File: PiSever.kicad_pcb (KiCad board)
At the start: 2 copper layers, 11 parts, among them J1 USB_C_Receptacle, J2 Fan, J3 BMP, J4 RX Ant, J5 TX Ant, P1 USB_C_Plug, U1 QFM-RX1-433, U2 AK-FST

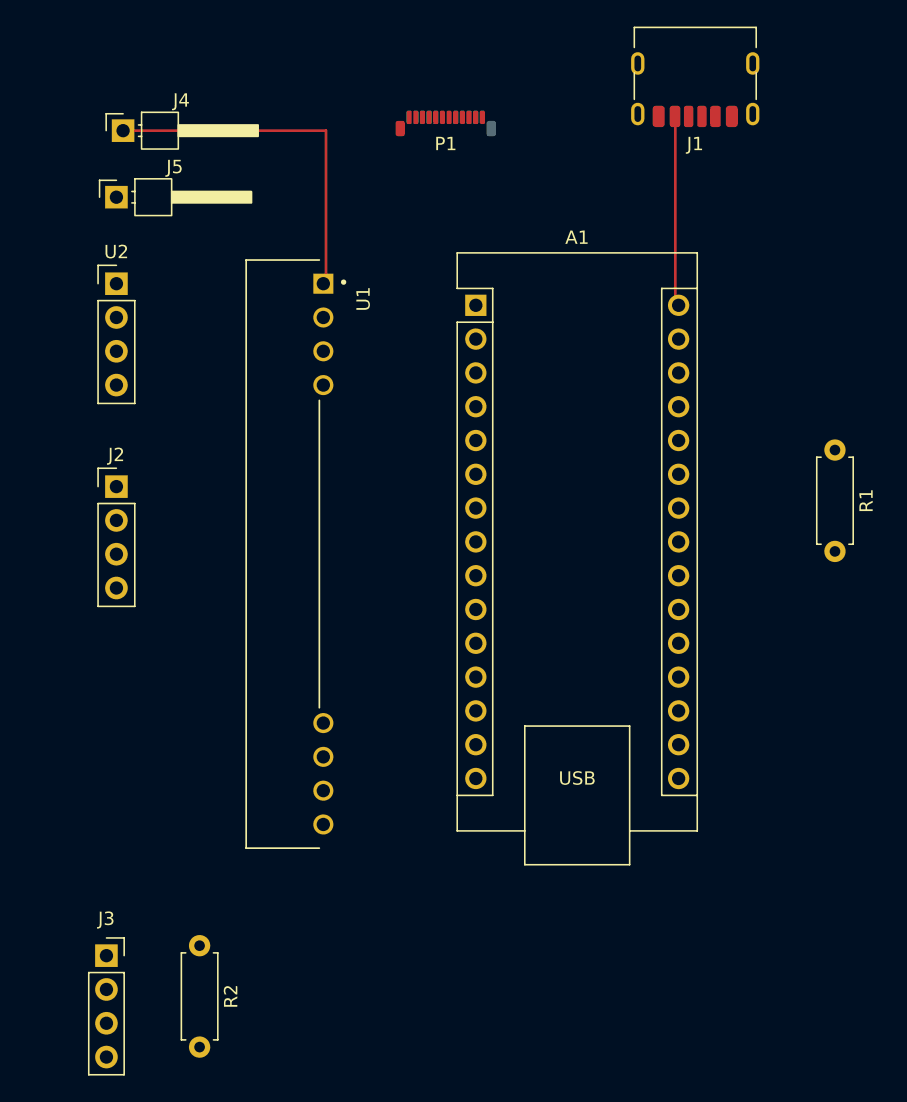
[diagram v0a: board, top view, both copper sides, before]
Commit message: Add through hole usb
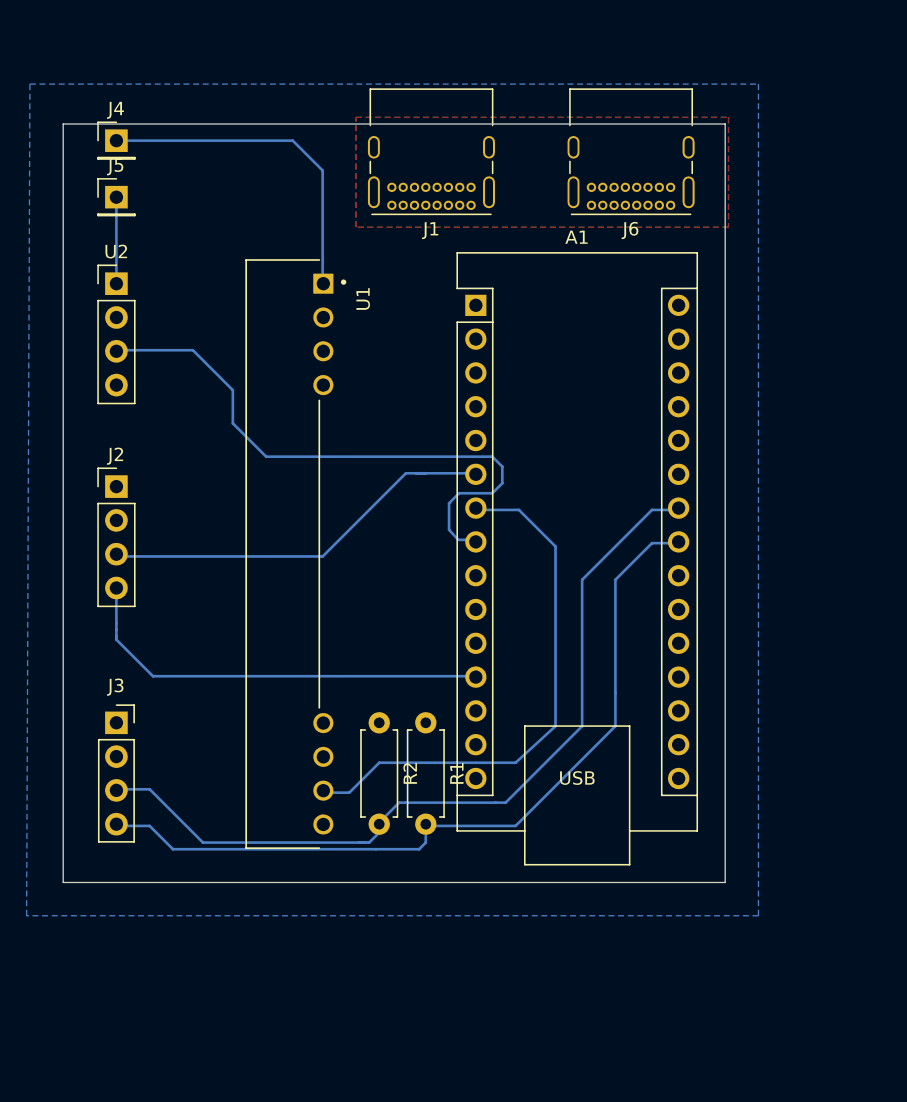
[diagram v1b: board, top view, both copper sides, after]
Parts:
- removed P1: USB_C_Plug, Connector_USB:USB_C_Plug_Molex_105444
- added J6: USB Power OUT, Connector_USB:USB_C_Receptacle_GCT_USB4085, F.Cu at (123.4, 66.6)
- J1: value USB_C_Receptacle -> USB Power IN; footprint Connector_USB:USB_C_Receptacle_HRO_TYPE-C-31-M-17 -> Connector_USB:USB_C_Receptacle_GCT_USB4085
- J4, J5: footprint Connector_PinHeader_2.54mm:PinHeader_1x01_P2.54mm_Horizontal -> Connector_PinHeader_2.54mm:PinHeader_1x01_P2.54mm_Vertical
- moved R1 37.0 mm to (105.0, 105.5)
- moved R2 21.5 mm to (101.5, 105.5)
- moved J1 19.5 mm to (108.4, 66.6)
- moved J3 17.5 mm to (81.8, 105.5)
- moved J4 0.90 mm to (81.8, 61.8)
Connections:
- J1 pad B5: unconnected-(J1-CC2-PadB5) -> Net-(J1-CC2)
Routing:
- added copper zone on F.Cu, net +5V
- added copper zone on B.Cu, net GND
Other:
- board outline added: 49.8 x 57 mm

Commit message: Re-route
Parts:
- removed R1, R2: R4.7k, Resistor_THT:R_Axial_DIN0207_L6.3mm_D2.5mm_P7.62mm_Horizontal
- moved J4 51.3 mm to (80.5, 113.0)
- moved U2 40.8 mm to (86.5, 113.0), turned to 180 degrees
- moved J5 39.5 mm to (80.5, 105.5)
- moved J3 33.5 mm to (80.5, 72.0), turned to 90 degrees
- moved J2 23.3 mm to (80.5, 64.5), turned to 90 degrees
- moved J1 3.40 mm to (111.8, 66.6)
- moved U1 2.30 mm to (96.5, 92.8), turned to 90 degrees
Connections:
- net Net-(A1-A4) renamed /SDA
- net Net-(A1-A5) renamed /SCL
- net Net-(A1-D3) renamed /FAN_TACH
- net Net-(A1-D9) renamed /FAN_PWM
- A1 pad 15: unconnected-(A1-D12-Pad15) -> Net-(A1-D12)
- A1 pad 27: unconnected-(A1-+5V-Pad27) -> /+5v_Arduino
- A1 pad 30: +5V -> unconnected-(A1-VIN-Pad30)
- A1 pad 5: unconnected-(A1-D2-Pad5) -> Net-(A1-D2)
- A1 pad 7: Net-(A1-D4) -> unconnected-(A1-D4-Pad7)
- A1 pad 8: Net-(A1-D5) -> unconnected-(A1-D5-Pad8)
- J3 pad 1: +5V -> /+5v_Arduino
- U1 pad 4: +5V -> /+5v_Arduino
- U1 pad 5: +5V -> /+5v_Arduino
- U1 pad 7: Net-(A1-D4) -> Net-(A1-D2)
- U2 pad 3: Net-(A1-D5) -> Net-(A1-D12)
- U2 pad 4: +5V -> /+5v_Arduino
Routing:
- net /+5v_Arduino: track 0.00 -> 73.9 mm
- net /FAN_PWM: track 0.00 -> 59.5 mm
- net /SCL: track 0.00 -> 54.9 mm
- net /SDA: track 0.00 -> 49.0 mm
- net /FAN_TACH: track 0.00 -> 45.9 mm
- net Net-(A1-D12): track 0.00 -> 23.0 mm
- net Net-(A1-D2): track 0.00 -> 19.1 mm
- net Net-(J4-Pin_1): track 0.00 -> 15.7 mm
- net Net-(J5-Pin_1): track 0.00 -> 11.5 mm
